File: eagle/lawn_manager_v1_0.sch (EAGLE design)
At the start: 15 parts, among them IC1 MEGA8-P, IC2 MAX232, K1 G2R, T1 BT138-H, T2 BT138-H

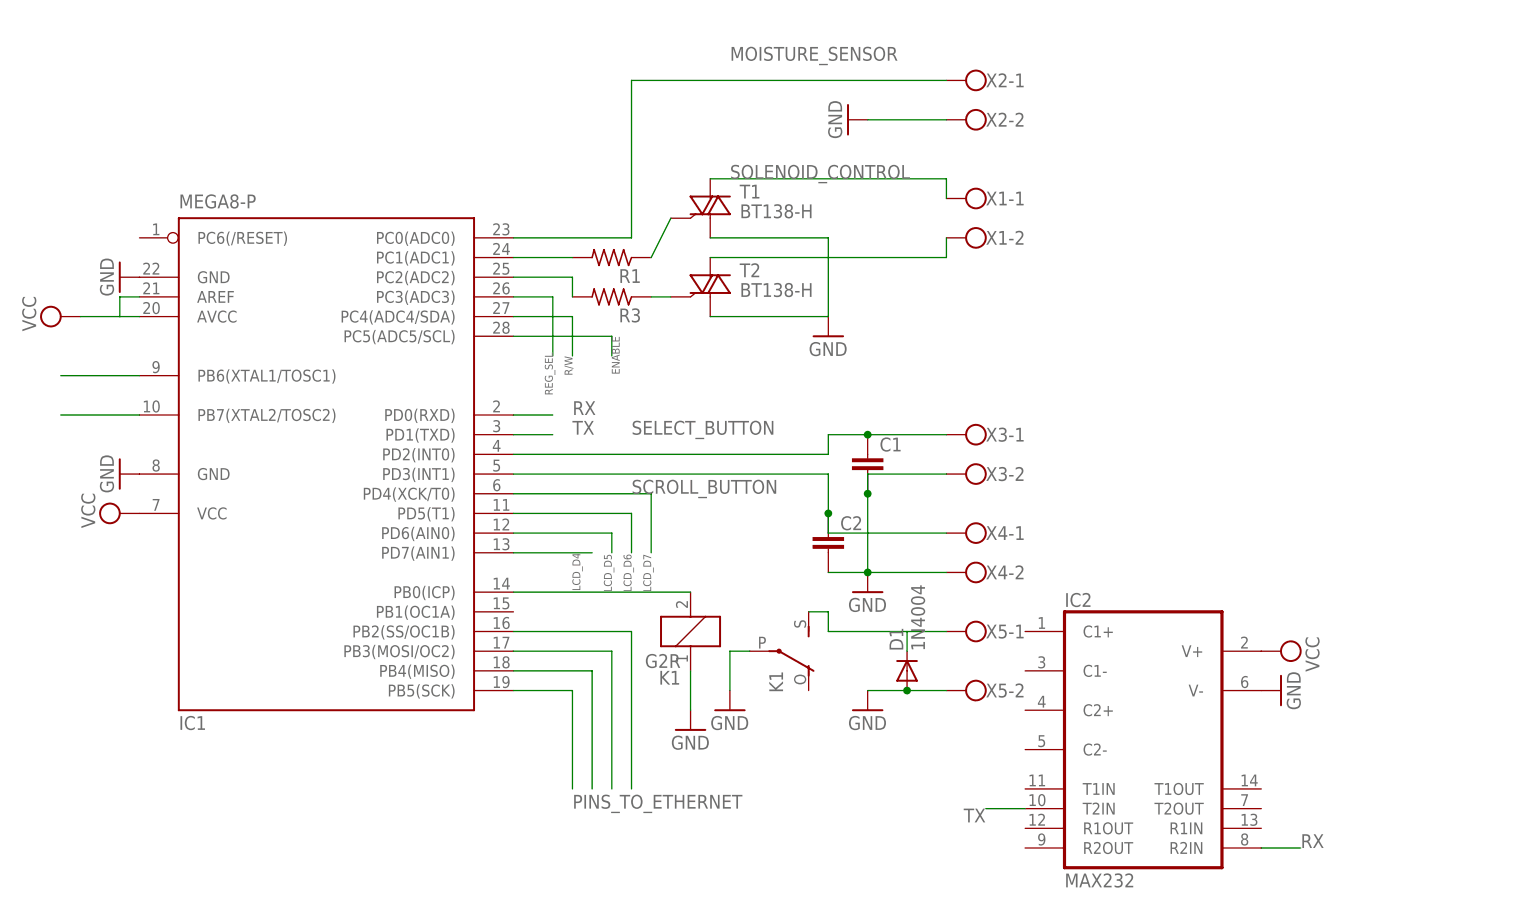
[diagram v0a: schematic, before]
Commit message: updated for RTC
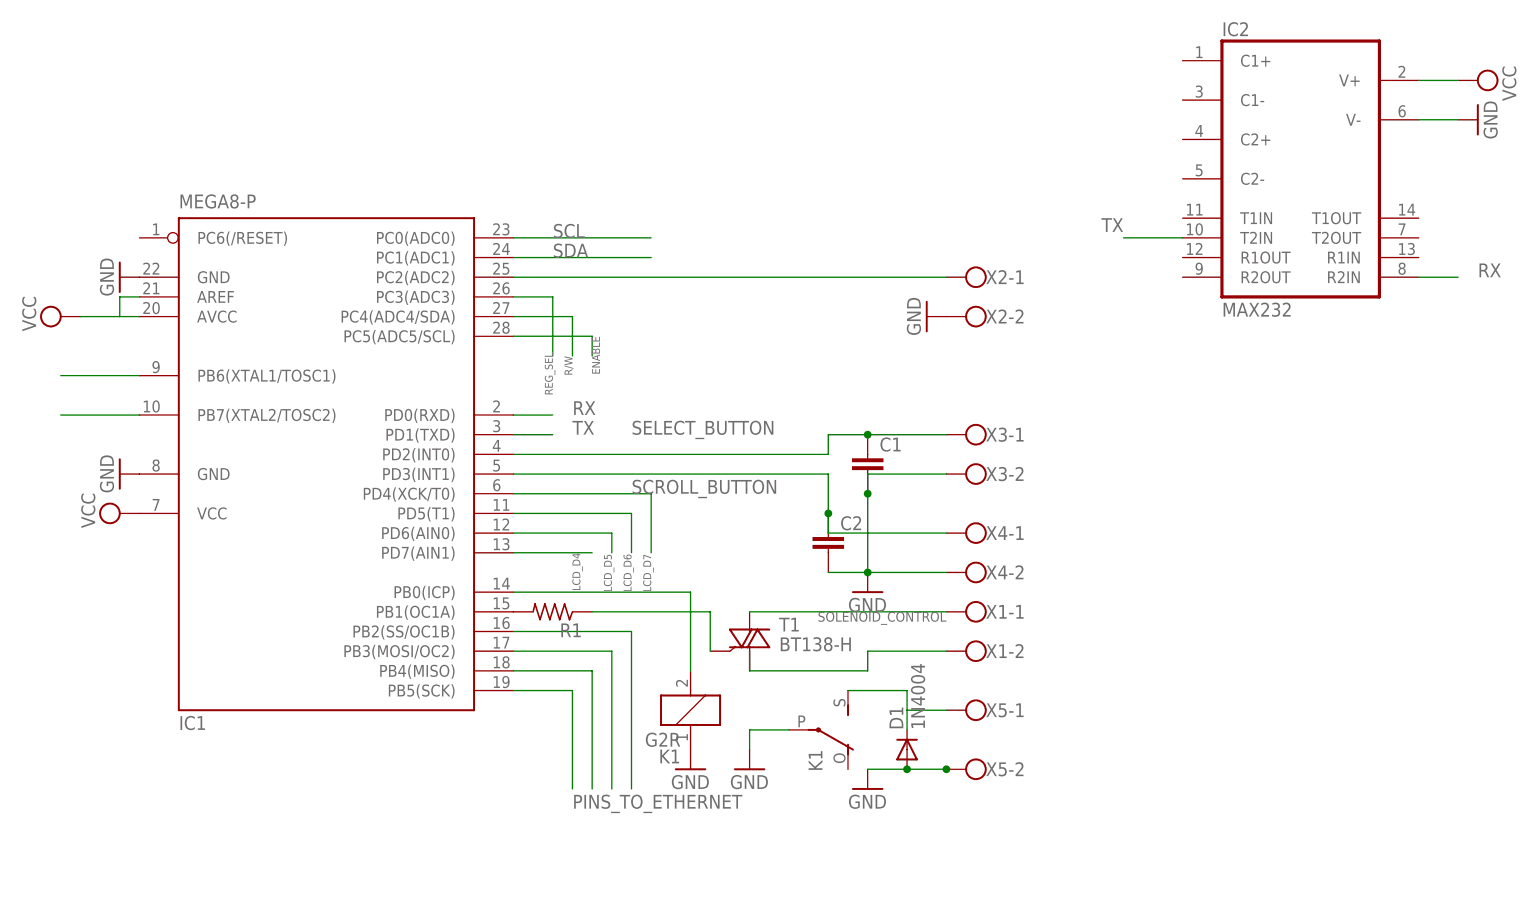
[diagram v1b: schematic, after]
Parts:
- removed R3: (no value), rcl:R-US_0207/10
- removed T2: BT138-H, triac:BT138-H
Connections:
- removed net MOISTURE_SENSOR: IC1.PC0(ADC0), X2-1.KL
- removed net N$10: R3.1, T2.G
- removed net N$9: IC1.PC2(ADC2), R3.2
- new net N$13: IC1.PC2(ADC2), X2-1.KL
- new net SCL: IC1.PC0(ADC0)
- new net SDA: IC1.PC1(ADC1)
- net GND: now also X5-2.KL; no longer T1.A1, T2.A1
- net N$3: now also IC1.PB1(OC1A); no longer IC1.PC1(ADC1)
- net N$8: now also T1.A1; no longer T2.A2
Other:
- moved on the sheet: D1, IC2, K1, R1, T1, X1-1, X1-2, X2-1, X2-2, X5-1, X5-2

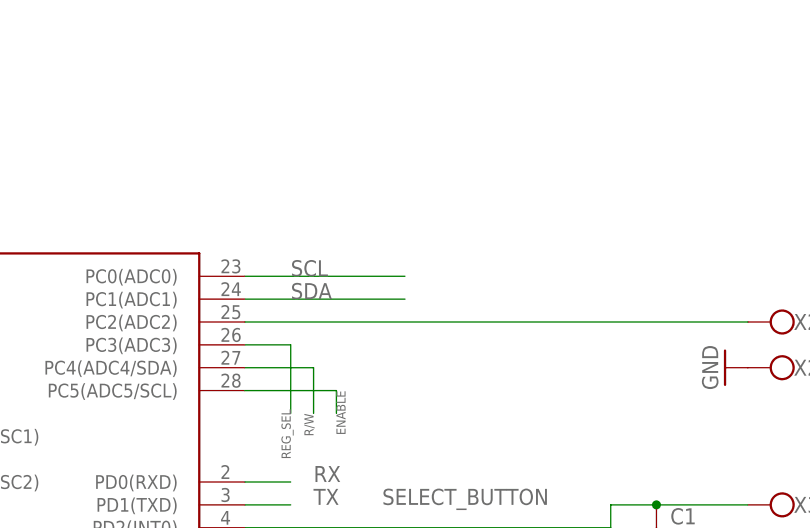
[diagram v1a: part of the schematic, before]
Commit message: ethernet and SPI libraries
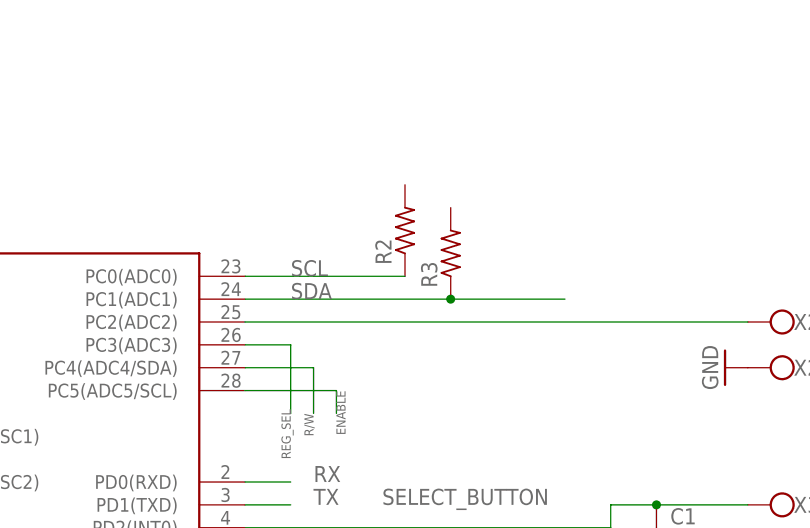
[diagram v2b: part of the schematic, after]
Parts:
- added R2, R3: (no value), rcl:R-US_0204/5
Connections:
- net SCL: now also R2.1
- net SDA: now also R3.1
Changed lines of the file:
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@@
 <part name="GND8" library="supply1" deviceset="GND" device=""/>
 <part name="GND9" library="supply1" deviceset="GND" device=""/>
+<part name="R2" library="rcl" deviceset="R-US_" device="0204/5"/>
+<part name="R3" library="rcl" deviceset="R-US_" device="0204/5"/>
 </parts>
 <sheets>
@@
 <instance part="GND8" gate="1" x="101.6" y="17.78"/>
 <instance part="GND9" gate="1" x="109.22" y="17.78"/>
+<instance part="R2" gate="G$1" x="96.52" y="91.44" rot="R90"/>
+<instance part="R3" gate="G$1" x="101.6" y="88.9" rot="R90"/>
 </instances>
 <busses>
@@
 <segment>
 <pinref part="IC1" gate="G$1" pin="PC1(ADC1)"/>
-<wire x1="78.74" y1="83.82" x2="96.52" y2="83.82" width="0.1524" layer="91"/>
 <label x="83.82" y="83.82" size="1.778" layer="91"/>
+<wire x1="78.74" y1="83.82" x2="101.6" y2="83.82" width="0.1524" layer="91"/>
+<pinref part="R3" gate="G$1" pin="1"/>
+<wire x1="101.6" y1="83.82" x2="114.3" y2="83.82" width="0.1524" layer="91"/>
+<junction x="101.6" y="83.82"/>
 </segment>
 </net>
@@
 <wire x1="78.74" y1="86.36" x2="96.52" y2="86.36" width="0.1524" layer="91"/>
 <label x="83.82" y="86.36" size="1.778" layer="91"/>
-</segment>
-</net>
+<pinref part="R2" gate="G$1" pin="1"/>
+</segment>
+</net>

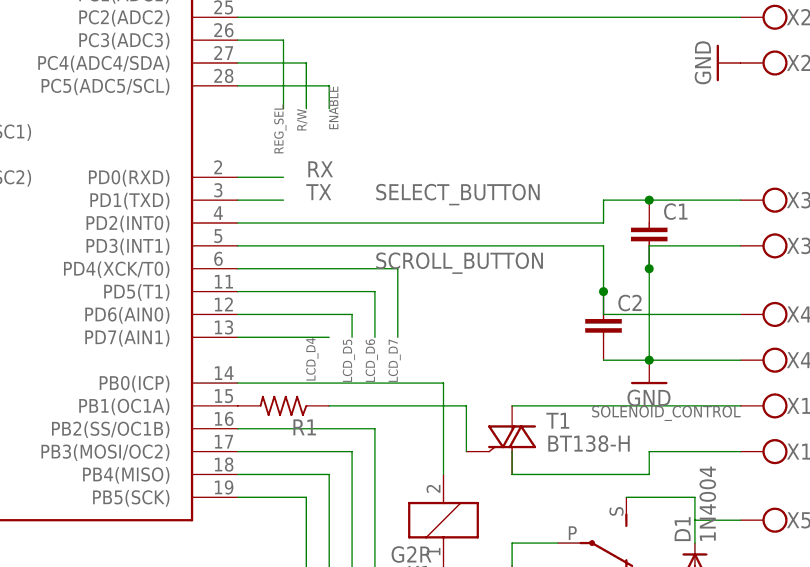
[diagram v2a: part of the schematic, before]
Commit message: working LCD code
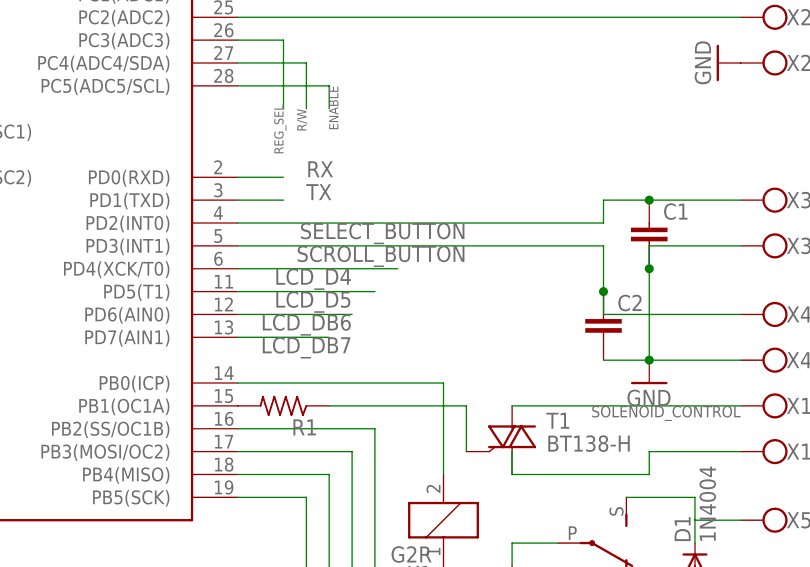
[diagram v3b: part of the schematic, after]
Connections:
- removed net LCD_D6: IC1.PD5(T1)
- removed net LCD_D7: IC1.PD4(XCK/T0)
- new net LCD_DB6: IC1.PD6(AIN0)
- new net LCD_DB7: IC1.PD7(AIN1)
- net LCD_D4: now also IC1.PD4(XCK/T0); no longer IC1.PD7(AIN1)
- net LCD_D5: now also IC1.PD5(T1); no longer IC1.PD6(AIN0)
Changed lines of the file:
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@@
 <net name="SELECT_BUTTON" class="0">
 <segment>
-<pinref part="IC1" gate="G$1" pin="PD2(INT0)"/>
-<wire x1="78.74" y1="58.42" x2="119.38" y2="58.42" width="0.1524" layer="91"/>
 <wire x1="119.38" y1="58.42" x2="119.38" y2="60.96" width="0.1524" layer="91"/>
 <wire x1="119.38" y1="60.96" x2="124.46" y2="60.96" width="0.1524" layer="91"/>
-<label x="93.98" y="60.96" size="1.778" layer="91"/>
 <pinref part="C1" gate="G$1" pin="1"/>
 <wire x1="124.46" y1="60.96" x2="134.62" y2="60.96" width="0.1524" layer="91"/>
 <junction x="124.46" y="60.96"/>
 <pinref part="X3" gate="-1" pin="KL"/>
+<pinref part="IC1" gate="G$1" pin="PD2(INT0)"/>
+<wire x1="78.74" y1="58.42" x2="119.38" y2="58.42" width="0.1524" layer="91"/>
+<label x="104.14" y="58.42" size="1.778" layer="95" rot="R180"/>
 </segment>
 </net>
@@
 <wire x1="119.38" y1="50.8" x2="119.38" y2="48.26" width="0.1524" layer="91"/>
 <wire x1="119.38" y1="48.26" x2="134.62" y2="48.26" width="0.1524" layer="91"/>
-<label x="93.98" y="53.34" size="1.778" layer="95"/>
 <pinref part="C2" gate="G$1" pin="1"/>
 <junction x="119.38" y="50.8"/>
 <pinref part="X4" gate="-1" pin="KL"/>
+<label x="104.14" y="55.88" size="1.778" layer="95" rot="R180"/>
 </segment>
 </net>
-<net name="LCD_D7" class="0">
+<net name="LCD_D4" class="0">
 <segment>
 <pinref part="IC1" gate="G$1" pin="PD4(XCK/T0)"/>
 <wire x1="78.74" y1="53.34" x2="96.52" y2="53.34" width="0.1524" layer="91"/>
-<wire x1="96.52" y1="53.34" x2="96.52" y2="45.72" width="0.1524" layer="91"/>
-<label x="96.52" y="40.64" size="1.016" layer="91" rot="R90"/>
-</segment>
-</net>
-<net name="LCD_D6" class="0">
-<segment>
-<pinref part="IC1" gate="G$1" pin="PD5(T1)"/>
-<wire x1="78.74" y1="50.8" x2="93.98" y2="50.8" width="0.1524" layer="91"/>
-<wire x1="93.98" y1="50.8" x2="93.98" y2="45.72" width="0.1524" layer="91"/>
-<label x="93.98" y="40.64" size="1.016" layer="91" rot="R90"/>
+<label x="91.44" y="53.34" size="1.778" layer="95" rot="R180"/>
 </segment>
 </net>
 <net name="LCD_D5" class="0">
 <segment>
+<pinref part="IC1" gate="G$1" pin="PD5(T1)"/>
+<wire x1="78.74" y1="50.8" x2="93.98" y2="50.8" width="0.1524" layer="91"/>
+<label x="91.44" y="50.8" size="1.778" layer="95" rot="R180"/>
+</segment>
+</net>
+<net name="LCD_DB6" class="0">
+<segment>
 <pinref part="IC1" gate="G$1" pin="PD6(AIN0)"/>
 <wire x1="78.74" y1="48.26" x2="91.44" y2="48.26" width="0.1524" layer="91"/>
-<wire x1="91.44" y1="48.26" x2="91.44" y2="45.72" width="0.1524" layer="91"/>
-<label x="91.44" y="40.64" size="1.016" layer="91" rot="R90"/>
-</segment>
-</net>
-<net name="LCD_D4" class="0">
-<segment>
-<pinref part="IC1" gate="G$1" pin="PD7(AIN1)"/>
-<wire x1="78.74" y1="45.72" x2="88.9" y2="45.72" width="0.1524" layer="91"/>
-<label x="86.36" y="45.72" size="1.016" layer="91" rot="R270"/>
+<label x="91.44" y="48.26" size="1.778" layer="95" rot="R180"/>
 </segment>
 </net>
@@
 <net name="N$12" class="0">
 <segment>
-<pinref part="IC1" gate="G$1" pin="PB0(ICP)"/>
 <pinref part="K1" gate="1" pin="2"/>
 <wire x1="101.6" y1="30.48" x2="101.6" y2="40.64" width="0.1524" layer="91"/>
-<wire x1="101.6" y1="40.64" x2="78.74" y2="40.64" width="0.1524" layer="91"/>
+<pinref part="IC1" gate="G$1" pin="PB0(ICP)"/>
+<wire x1="78.74" y1="40.64" x2="101.6" y2="40.64" width="0.1524" layer="91"/>
 </segment>
 </net>
@@
 </segment>
 </net>
+<net name="LCD_DB7" class="0">
+<segment>
+<pinref part="IC1" gate="G$1" pin="PD7(AIN1)"/>
+<wire x1="78.74" y1="45.72" x2="88.9" y2="45.72" width="0.1524" layer="91"/>
+<label x="91.44" y="45.72" size="1.778" layer="95" rot="R180"/>
+</segment>
+</net>
